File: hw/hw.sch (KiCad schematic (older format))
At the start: 8 parts, among them U1 74LS595, U2 74LS138, U3 Z80CPU, U4 74LS161, U5 CY7C199, X1 CXO_DIP8

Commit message: WIP: start thinking how Arduino can respond to port requests
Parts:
- removed U1: 74LS595, symbol 74xx:74LS595
- added U?: 74LS299, symbol 74xx:74LS299
- added U? (x2): 74LS74, symbol 74xx:74LS74
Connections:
- net labels added: SR_CLK, SR_MODE, SR_OUT, ~IO_ACK, ~IO_REQ, ~WAIT
- net labels removed: SR_RCLK, SR_SRCLK
- wire segments 145 -> 162
- no-connect marks 36 -> 33
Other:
- moved on the sheet: U2

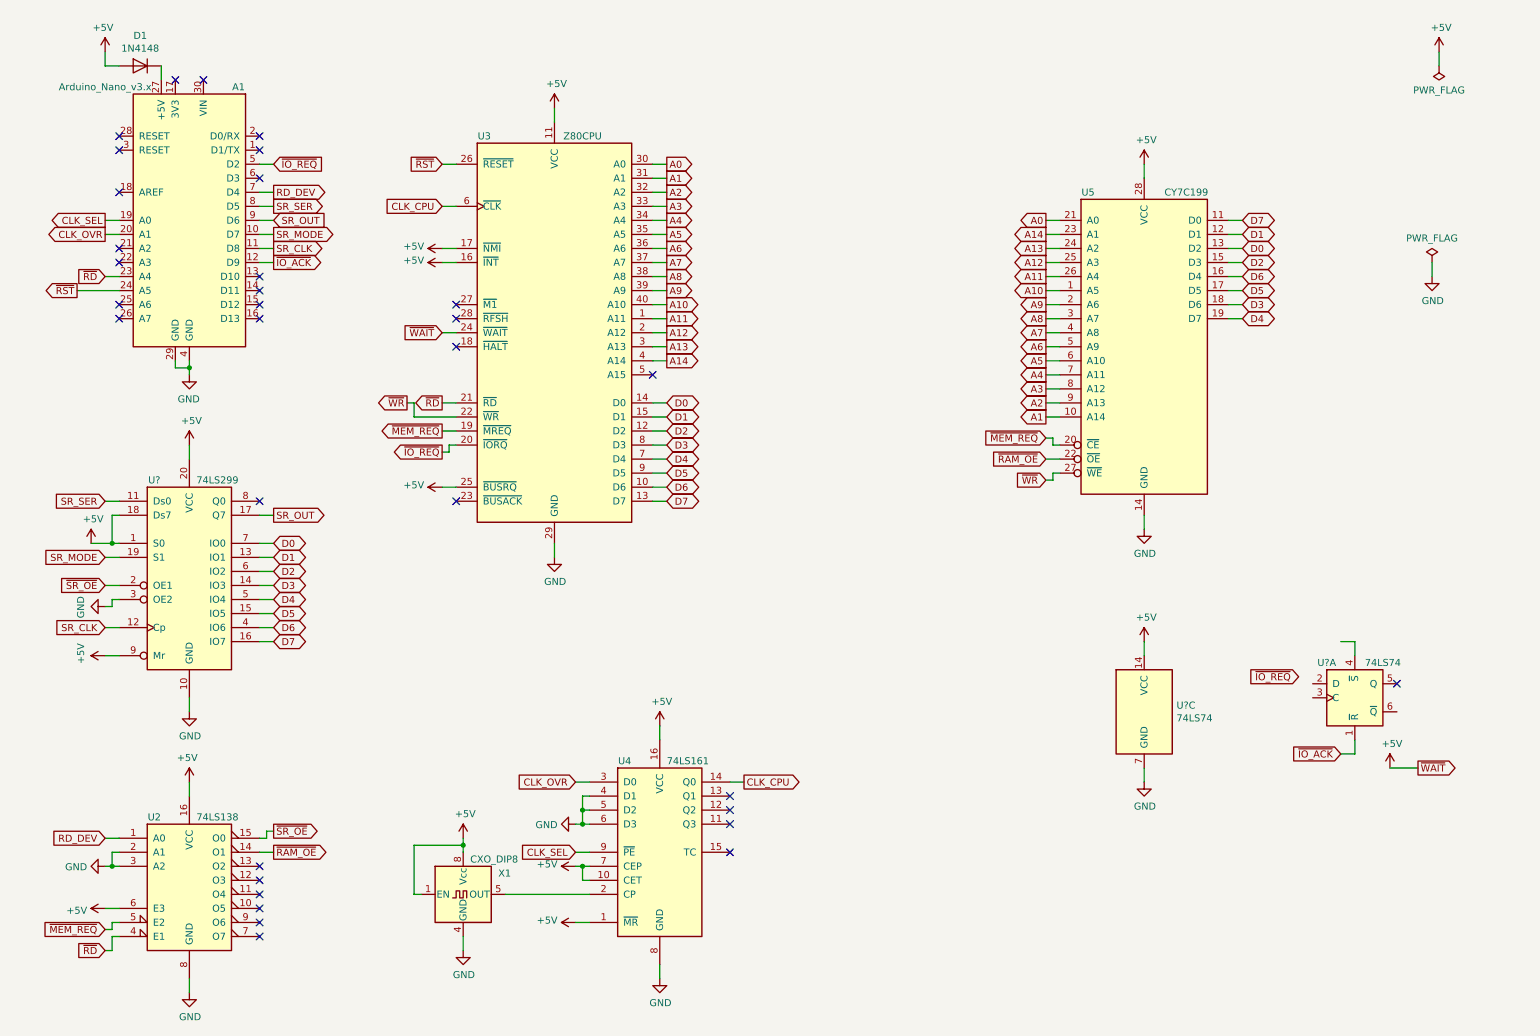
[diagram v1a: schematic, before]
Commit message: got IO port writing working
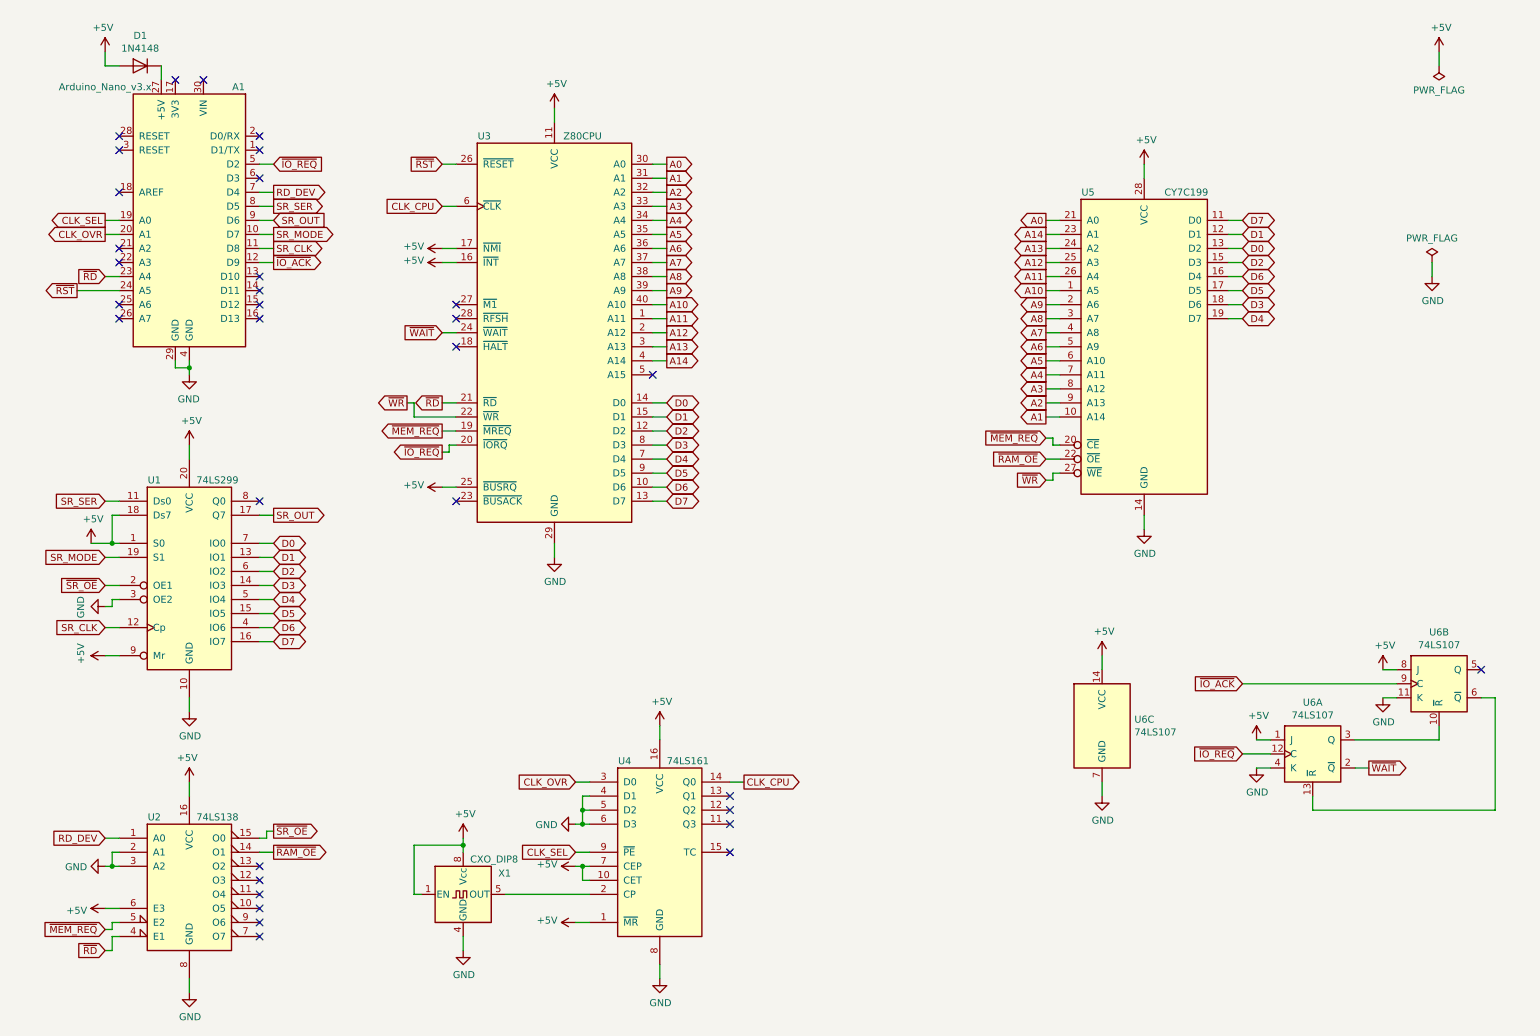
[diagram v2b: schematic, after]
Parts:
- removed U? (x2): 74LS74, symbol 74xx:74LS74
- added U6: 74LS107, symbol 74xx:74LS107
- gave numbers to parts that had none: 1
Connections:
- net +5V: now also U6.1 (J), U6.14 (VCC), U6.8 (J); no longer U3.24 (~WAIT~)
- net GND: now also U6.11 (K), U6.4 (K), U6.7 (GND)
- net ~IO_ACK: now also U6.9 (C)
- net ~IO_REQ: now also U6.12 (C)
- new net: U6.13 (~R), U6.6 (~Q)
- new net: U6.10 (~R), U6.3 (Q)
- new net ~WAIT: U3.24 (~WAIT~), U6.2 (~Q)
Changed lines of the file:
@@
 	3950 6800 4550 6800
 $Comp
-L power:PWR_FLAG #FLG?
+L power:PWR_FLAG #FLG01
 U 1 1 5D4751A2
 P 10550 2300
-F 0 "#FLG?" H 10550 2375 50  0001 C CNN
+F 0 "#FLG01" H 10550 2375 50  0001 C CNN
 F 1 "PWR_FLAG" H 10550 2473 50  0000 C CNN
 F 2 "" H 10550 2300 50  0001 C CNN
@@
 	10550 2300 10550 2400
 $Comp
-L power:GND #PWR?
+L power:GND #PWR012
 U 1 1 5D489F33
 P 10550 2400
-F 0 "#PWR?" H 10550 2150 50  0001 C CNN
+F 0 "#PWR012" H 10550 2150 50  0001 C CNN
 F 1 "GND" H 10555 2227 50  0000 C CNN
 F 2 "" H 10550 2400 50  0001 C CNN
@@
 $EndComp
 $Comp
-L 74xx:74LS299 U?
+L 74xx:74LS299 U1
 U 1 1 5D2A7D49
 P 1700 4500
-F 0 "U?" H 1450 5150 50  0000 C CNN
+F 0 "U1" H 1450 5150 50  0000 C CNN
 F 1 "74LS299" H 1900 5150 50  0000 C CNN
 F 2 "" H 1700 4500 50  0001 C CNN
@@
 	1100 4000 1200 4000
 $Comp
-L power:+5V #PWR?
+L power:+5V #PWR04
 U 1 1 5D2C9E11
 P 1700 3600
-F 0 "#PWR?" H 1700 3450 50  0001 C CNN
+F 0 "#PWR04" H 1700 3450 50  0001 C CNN
 F 1 "+5V" H 1715 3773 50  0000 C CNN
 F 2 "" H 1700 3600 50  0001 C CNN
@@
 	1700 3600 1700 3700
 $Comp
-L power:GND #PWR?
+L power:GND #PWR05
 U 1 1 5D2D28C6
 P 1700 5500
-F 0 "#PWR?" H 1700 5250 50  0001 C CNN
+F 0 "#PWR05" H 1700 5250 50  0001 C CNN
 F 1 "GND" H 1705 5327 50  0000 C CNN
 F 2 "" H 1700 5500 50  0001 C CNN
@@
 	1700 5400 1700 5500
 $Comp
-L power:+5V #PWR?
+L power:+5V #PWR01
 U 1 1 5D2DB444
 P 1000 4300
-F 0 "#PWR?" H 1000 4150 50  0001 C CNN
+F 0 "#PWR01" H 1000 4150 50  0001 C CNN
 F 1 "+5V" H 1015 4473 50  0000 C CNN
 F 2 "" H 1000 4300 50  0001 C CNN
@@
 	1100 4600 1200 4600
 $Comp
-L power:GND #PWR?
+L power:GND #PWR02
 U 1 1 5D3095DE
 P 1100 4750
-F 0 "#PWR?" H 1100 4500 50  0001 C CNN
+F 0 "#PWR02" H 1100 4500 50  0001 C CNN
 F 1 "GND" H 1105 4577 50  0000 C CNN
 F 2 "" H 1100 4750 50  0001 C CNN
@@
 	1100 4900 1200 4900
 $Comp
-L power:+5V #PWR?
+L power:+5V #PWR03
 U 1 1 5D31DBB1
 P 1100 5100
-F 0 "#PWR?" H 1100 4950 50  0001 C CNN
+F 0 "#PWR03" H 1100 4950 50  0001 C CNN
 F 1 "+5V" H 1115 5273 50  0000 C CNN
 F 2 "" H 1100 5100 50  0001 C CNN
@@
 	2200 2000 2300 2000
 $Comp
-L 74xx:74LS74 U?
-U 1 1 5D349635
-P 10000 5400
-F 0 "U?" H 9800 5650 50  0000 C CNN
-F 1 "74LS74" H 10200 5650 50  0000 C CNN
-F 2 "" H 10000 5400 50  0001 C CNN
-F 3 "74xx/74hc_hct74.pdf" H 10000 5400 50  0001 C CNN
-	1    10000 5400
-	1    0    0    -1
-$EndComp
-$Comp
-L 74xx:74LS74 U?
-U 3 1 5D3496BD
-P 8500 5500
-F 0 "U?" H 8730 5546 50  0000 L CNN
-F 1 "74LS74" H 8730 5455 50  0000 L CNN
-F 2 "" H 8500 5500 50  0001 C CNN
-F 3 "74xx/74hc_hct74.pdf" H 8500 5500 50  0001 C CNN
-	3    8500 5500
-	1    0    0    -1
-$EndComp
-$Comp
-L power:+5V #PWR?
+L power:+5V #PWR06
 U 1 1 5D349977
-P 8500 5000
-F 0 "#PWR?" H 8500 4850 50  0001 C CNN
-F 1 "+5V" H 8515 5173 50  0000 C CNN
-F 2 "" H 8500 5000 50  0001 C CNN
-F 3 "" H 8500 5000 50  0001 C CNN
-	1    8500 5000
-	1    0    0    -1
-$EndComp
-$Comp
-L power:GND #PWR?
+P 8200 5100
+F 0 "#PWR06" H 8200 4950 50  0001 C CNN
+F 1 "+5V" H 8215 5273 50  0000 C CNN
+F 2 "" H 8200 5100 50  0001 C CNN
+F 3 "" H 8200 5100 50  0001 C CNN
+	1    8200 5100
+	1    0    0    -1
+$EndComp
+$Comp
+L power:GND #PWR07
 U 1 1 5D349996
-P 8500 6000
-F 0 "#PWR?" H 8500 5750 50  0001 C CNN
-F 1 "GND" H 8505 5827 50  0000 C CNN
-F 2 "" H 8500 6000 50  0001 C CNN
-F 3 "" H 8500 6000 50  0001 C CNN
-	1    8500 6000
-	1    0    0    -1
-$EndComp
-Wire Wire Line
-	8500 5900 8500 6000
-Wire Wire Line
-	8500 5000 8500 5100
+P 8200 6100
+F 0 "#PWR07" H 8200 5850 50  0001 C CNN
+F 1 "GND" H 8205 5927 50  0000 C CNN
+F 2 "" H 8200 6100 50  0001 C CNN
+F 3 "" H 8200 6100 50  0001 C CNN
+	1    8200 6100
+	1    0    0    -1
+$EndComp
+Wire Wire Line
+	8200 6000 8200 6100
+Wire Wire Line
+	8200 5100 8200 5200
 Text GLabel 3500 3650 0    50   Output ~ 0
 ~IO_REQ
@@
 Wire Wire Line
 	3550 3650 3500 3650
-Text GLabel 9600 5250 0    50   Input ~ 0
+Text GLabel 9200 5800 0    50   Input ~ 0
 ~IO_REQ
-Wire Wire Line
-	9900 5000 10000 5000
-Wire Wire Line
-	10000 5000 10000 5100
 Text GLabel 3500 2800 0    50   Input ~ 0
 ~WAIT
-Text GLabel 10450 5900 2    50   Output ~ 0
+Text GLabel 10100 5900 2    50   Output ~ 0
 ~WAIT
-Text GLabel 9900 5800 0    50   Input ~ 0
+Text GLabel 9200 5300 0    50   Input ~ 0
 ~IO_ACK
-Wire Wire Line
-	9900 5800 10000 5800
-Wire Wire Line
-	10000 5800 10000 5700
-NoConn ~ 10300 5300
 Text GLabel 2300 2300 2    50   Output ~ 0
 ~IO_ACK
@@
 	2300 1600 2200 1600
 $Comp
-L power:+5V #PWR?
+L power:+5V #PWR08
 U 1 1 5D3F14DC
-P 10250 5900
-F 0 "#PWR?" H 10250 5750 50  0001 C CNN
-F 1 "+5V" H 10265 6073 50  0000 C CNN
-F 2 "" H 10250 5900 50  0001 C CNN
-F 3 "" H 10250 5900 50  0001 C CNN
-	1    10250 5900
-	1    0    0    -1
-$EndComp
-Wire Wire Line
-	10250 5900 10450 5900
+P 9300 5700
+F 0 "#PWR08" H 9300 5550 50  0001 C CNN
+F 1 "+5V" H 9315 5873 50  0000 C CNN
+F 2 "" H 9300 5700 50  0001 C CNN
+F 3 "" H 9300 5700 50  0001 C CNN
+	1    9300 5700
+	1    0    0    -1
+$EndComp
+$Comp
+L 74xx:74LS107 U6
+U 1 1 5D403DD8
+P 9700 5800
+F 0 "U6" H 9700 6167 50  0000 C CNN
+F 1 "74LS107" H 9700 6076 50  0000 C CNN
+F 2 "" H 9700 5800 50  0001 C CNN
+F 3 "http://www.ti.com/lit/gpn/sn74LS107" H 9700 5800 50  0001 C CNN
+	1    9700 5800
+	1    0    0    -1
+$EndComp
+$Comp
+L 74xx:74LS107 U6
+U 2 1 5D403E46
+P 10600 5300
+F 0 "U6" H 10600 5667 50  0000 C CNN
+F 1 "74LS107" H 10600 5576 50  0000 C CNN
+F 2 "" H 10600 5300 50  0001 C CNN
+F 3 "http://www.ti.com/lit/gpn/sn74LS107" H 10600 5300 50  0001 C CNN
+	2    10600 5300
+	1    0    0    -1
+$EndComp
+$Comp
+L 74xx:74LS107 U6
+U 3 1 5D403EC1
+P 8200 5600
+F 0 "U6" H 8430 5646 50  0000 L CNN
+F 1 "74LS107" H 8430 5555 50  0000 L CNN
+F 2 "" H 8200 5600 50  0001 C CNN
+F 3 "http://www.ti.com/lit/gpn/sn74LS107" H 8200 5600 50  0001 C CNN
+	3    8200 5600
+	1    0    0    -1
+$EndComp
+$Comp
+L power:GND #PWR09
+U 1 1 5D403FBF
+P 9300 5900
+F 0 "#PWR09" H 9300 5650 50  0001 C CNN
+F 1 "GND" H 9305 5727 50  0000 C CNN
+F 2 "" H 9300 5900 50  0001 C CNN
+F 3 "" H 9300 5900 50  0001 C CNN
+	1    9300 5900
+	1    0    0    -1
+$EndComp
+Wire Wire Line
+	9300 5900 9400 5900
+Wire Wire Line
+	9400 5700 9300 5700
+Wire Wire Line
+	10100 5900 10000 5900
+$Comp
+L power:+5V #PWR010
+U 1 1 5D41FA3B
+P 10200 5200
+F 0 "#PWR010" H 10200 5050 50  0001 C CNN
+F 1 "+5V" H 10215 5373 50  0000 C CNN
+F 2 "" H 10200 5200 50  0001 C CNN
+F 3 "" H 10200 5200 50  0001 C CNN
+	1    10200 5200
+	1    0    0    -1
+$EndComp
+$Comp
+L power:GND #PWR011
+U 1 1 5D41FA41
+P 10200 5400
+F 0 "#PWR011" H 10200 5150 50  0001 C CNN
+F 1 "GND" H 10205 5227 50  0000 C CNN
+F 2 "" H 10200 5400 50  0001 C CNN
+F 3 "" H 10200 5400 50  0001 C CNN
+	1    10200 5400
+	1    0    0    -1
+$EndComp
+Wire Wire Line
+	10200 5400 10300 5400
+Wire Wire Line
+	10300 5200 10200 5200
+Wire Wire Line
+	10600 5600 10600 5700
+Wire Wire Line
+	10600 5700 10000 5700
+Wire Wire Line
+	10900 5400 11000 5400
+Wire Wire Line
+	11000 5400 11000 6200
+Wire Wire Line
+	11000 6200 9700 6200
+Wire Wire Line
+	9700 6200 9700 6100
+Wire Wire Line
+	9200 5800 9400 5800
+Wire Wire Line
+	9200 5300 10300 5300
+NoConn ~ 10900 5200
 $EndSCHEMATC

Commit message: update schematic cache
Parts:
- added R?: 47K, symbol Device:R
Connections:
- net GND: now also R?.1
- net ~RST: now also R?.2
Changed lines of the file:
@@
 	9200 5300 10300 5300
 NoConn ~ 10900 5200
+Text GLabel 6000 1400 0    50   Output ~ 0
+~RST
+$Comp
+L Device:R R?
+U 1 1 5D4A0E06
+P 6250 1400
+F 0 "R?" V 6043 1400 50  0000 C CNN
+F 1 "47K" V 6134 1400 50  0000 C CNN
+F 2 "" V 6180 1400 50  0001 C CNN
+F 3 "~" H 6250 1400 50  0001 C CNN
+	1    6250 1400
+	0    1    1    0
+$EndComp
+Wire Wire Line
+	6500 1400 6400 1400
+Wire Wire Line
+	6100 1400 6000 1400
+$Comp
+L power:GND #PWR?
+U 1 1 5D4B4F94
+P 6500 1400
+F 0 "#PWR?" H 6500 1150 50  0001 C CNN
+F 1 "GND" H 6505 1227 50  0000 C CNN
+F 2 "" H 6500 1400 50  0001 C CNN
+F 3 "" H 6500 1400 50  0001 C CNN
+	1    6500 1400
+	1    0    0    -1
+$EndComp
 $EndSCHEMATC
